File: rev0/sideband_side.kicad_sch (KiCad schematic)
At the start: 28 parts, among them IC1 ECP5-BGA256, U8 USB3343-CP

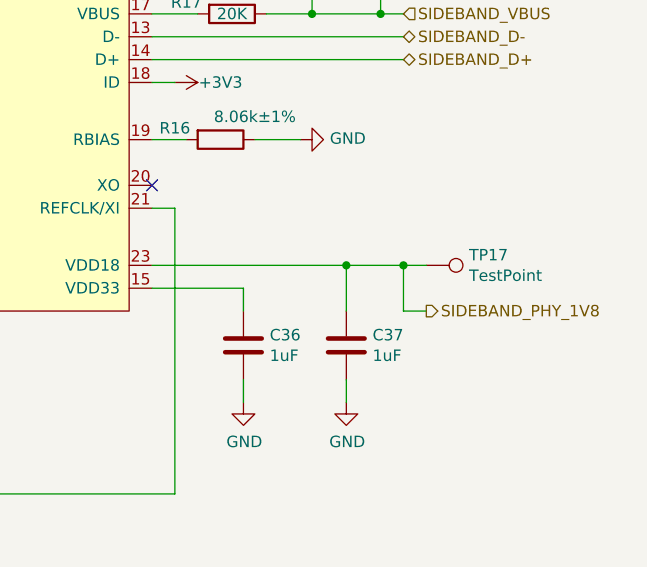
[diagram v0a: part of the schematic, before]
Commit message: hardware: remove PHY 1.8 V measurement
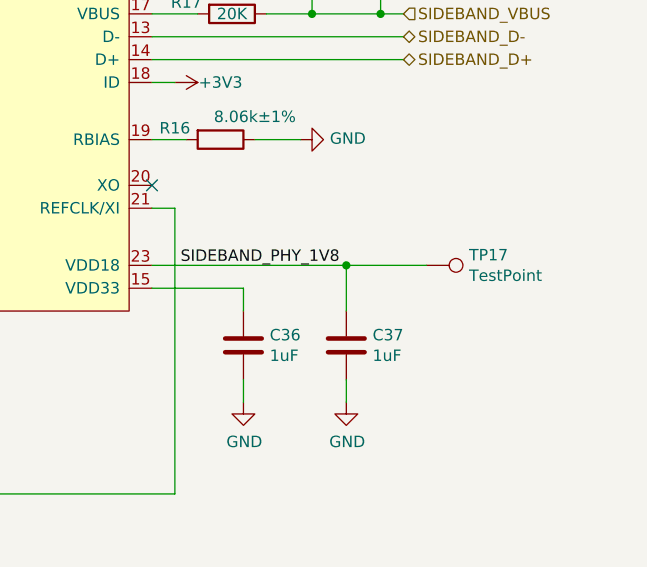
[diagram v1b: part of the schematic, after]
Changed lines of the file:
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@@
   (junction (at 33.02 64.77) (diameter 0) (color 0 0 0 0)
-  )
-  (junction (at 254 124.46) (diameter 0) (color 0 0 0 0)
   )
   (junction (at 46.99 52.07) (diameter 0) (color 0 0 0 0)
@@
     (stroke (width 0) (type default) (color 0 0 0 0))
   )
-  (wire (pts (xy 247.65 124.46) (xy 254 124.46))
+  (wire (pts (xy 247.65 124.46) (xy 256.54 124.46))
     (stroke (width 0) (type default) (color 0 0 0 0))
   )
@@
     (stroke (width 0) (type default) (color 0 0 0 0))
   )
-  (wire (pts (xy 254 124.46) (xy 256.54 124.46))
-    (stroke (width 0) (type default) (color 0 0 0 0))
-  )
   (wire (pts (xy 85.09 34.29) (xy 90.17 34.29))
     (stroke (width 0) (type default) (color 0 0 0 0))
@@
     (stroke (width 0) (type default) (color 0 0 0 0))
   )
-  (wire (pts (xy 254 129.54) (xy 254 124.46))
-    (stroke (width 0) (type default) (color 0 0 0 0))
-  )
   (wire (pts (xy 68.58 49.53) (xy 68.58 52.07))
     (stroke (width 0) (type default) (color 0 0 0 0))
@@
     (stroke (width 0) (type default) (color 0 0 0 0))
   )
-  (wire (pts (xy 256.54 129.54) (xy 254 129.54))
-    (stroke (width 0) (type default) (color 0 0 0 0))
-  )
   (wire (pts (xy 119.38 157.48) (xy 151.13 157.48))
     (stroke (width 0) (type default) (color 0 0 0 0))
@@
   )
   (label "SIDEBAND_DATA3" (at 168.91 93.98 0)
+    (effects (font (size 1.27 1.27)) (justify left bottom))
+  )
+  (label "SIDEBAND_PHY_1V8" (at 229.235 124.46 0)
     (effects (font (size 1.27 1.27)) (justify left bottom))
   )
@@
     (effects (font (size 1.27 1.27)) (justify left))
   )
-  (hierarchical_label "SIDEBAND_PHY_1V8" (shape output) (at 256.54 129.54 0)
-    (effects (font (size 1.27 1.27)) (justify left))
-  )

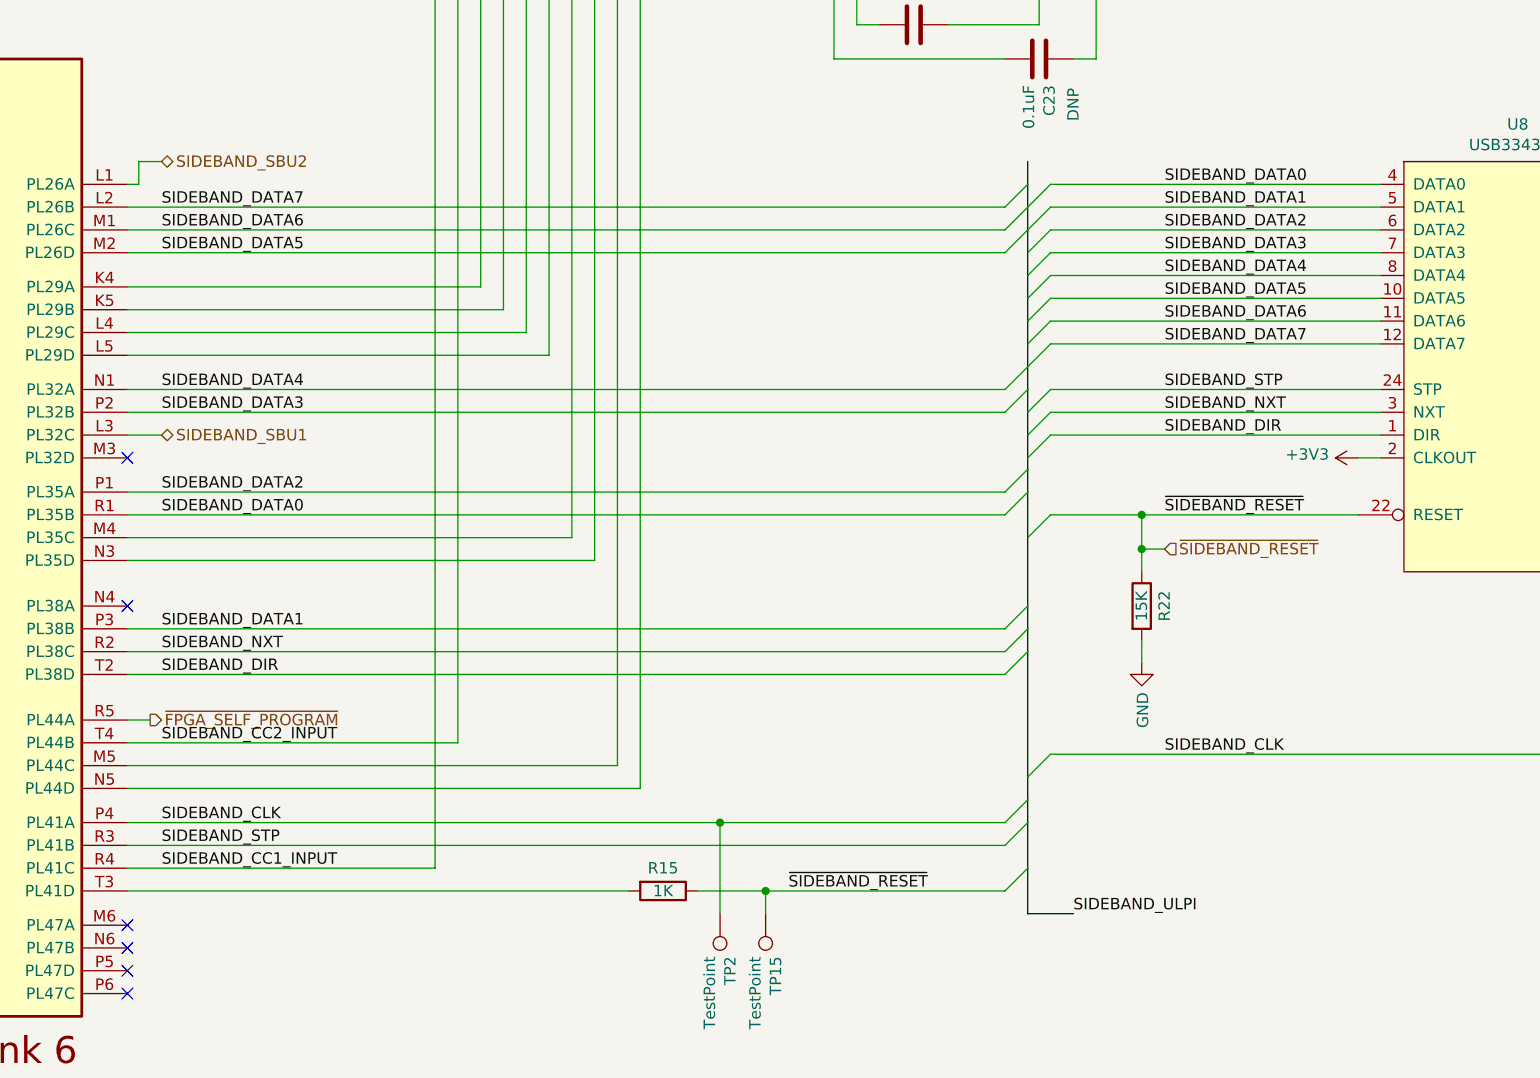
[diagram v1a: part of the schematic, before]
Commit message: hardware: rename buses for KiCad 6
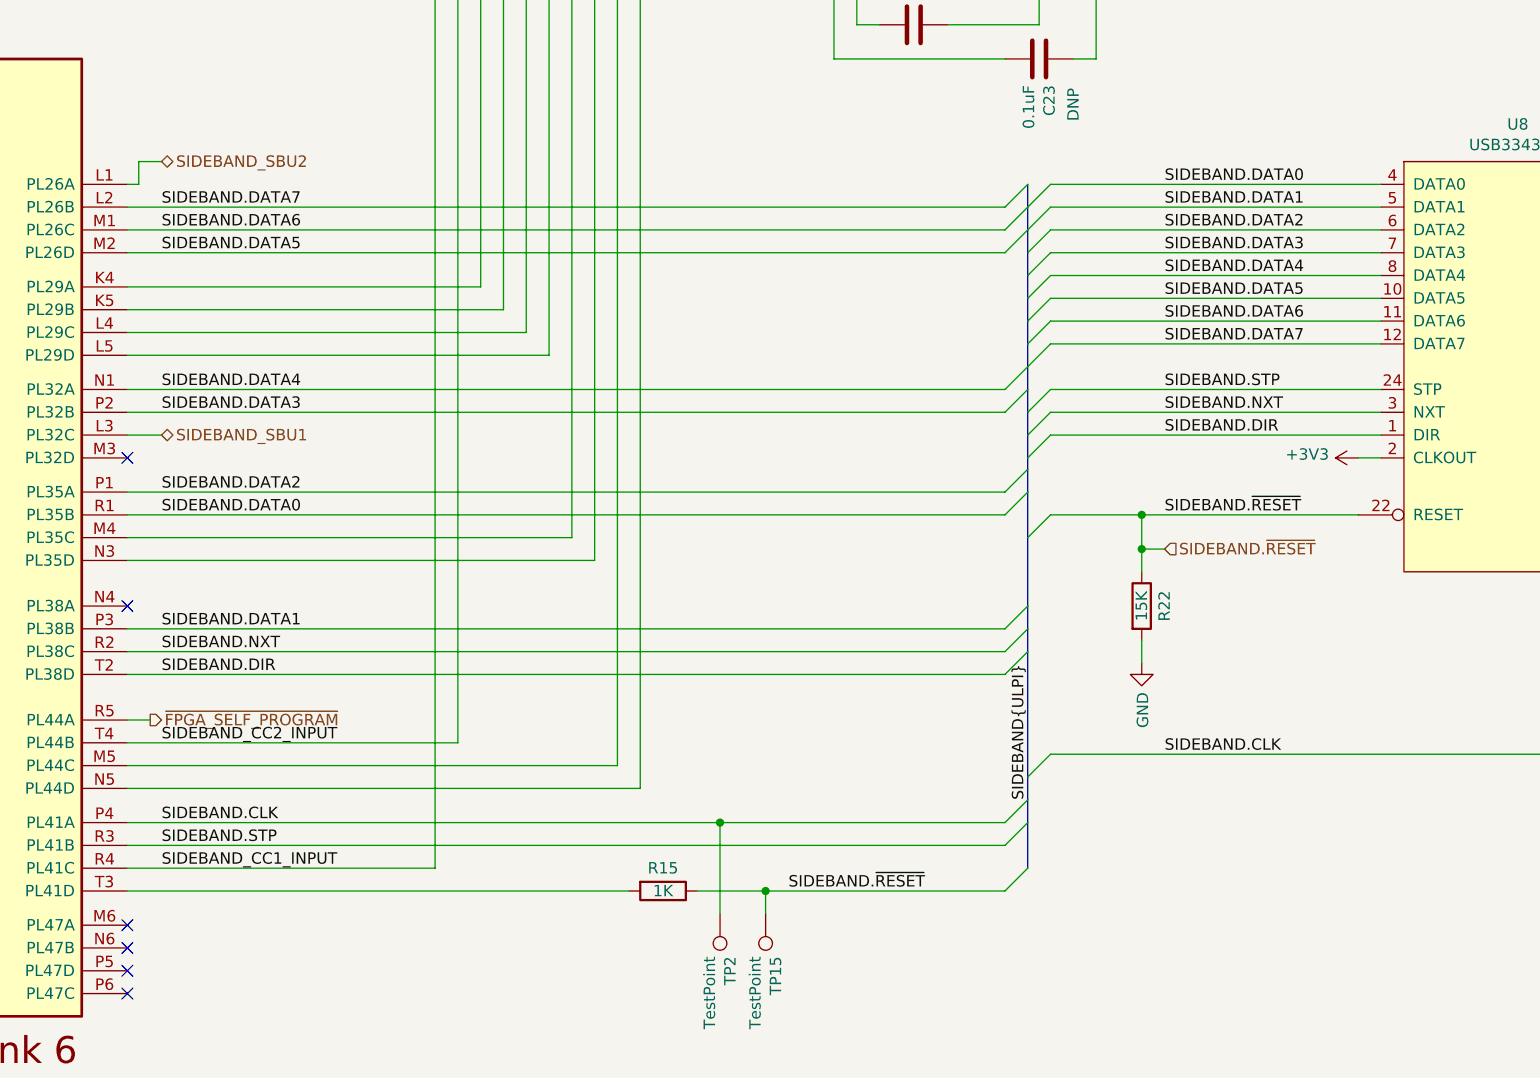
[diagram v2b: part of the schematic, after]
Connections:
- net SIDEBAND_CLK renamed SIDEBAND.CLK
- net SIDEBAND_DATA0 renamed SIDEBAND.DATA0
- net SIDEBAND_DATA1 renamed SIDEBAND.DATA1
- net SIDEBAND_DATA2 renamed SIDEBAND.DATA2
- net SIDEBAND_DATA3 renamed SIDEBAND.DATA3
- net SIDEBAND_DATA4 renamed SIDEBAND.DATA4
- net SIDEBAND_DATA5 renamed SIDEBAND.DATA5
- net SIDEBAND_DATA6 renamed SIDEBAND.DATA6
- net SIDEBAND_DATA7 renamed SIDEBAND.DATA7
- net SIDEBAND_DIR renamed SIDEBAND.DIR
- net SIDEBAND_NXT renamed SIDEBAND.NXT
- net SIDEBAND_STP renamed SIDEBAND.STP
- net ~{SIDEBAND_RESET} renamed SIDEBAND.~{RESET}
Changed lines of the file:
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@@
-    (stroke (width 0) (type default) (color 0 0 0 0))
-  )
-  (bus (pts (xy 153.67 162.56) (xy 153.67 167.64))
     (stroke (width 0) (type default) (color 0 0 0 0))
   )
@@
     (stroke (width 0) (type default) (color 0 0 0 0))
   )
-  (bus (pts (xy 153.67 83.82) (xy 153.67 86.36))
-    (stroke (width 0) (type default) (color 0 0 0 0))
-  )
   (wire (pts (xy 144.78 39.37) (xy 165.1 39.37))
     (stroke (width 0) (type default) (color 0 0 0 0))
@@
     (stroke (width 0) (type default) (color 0 0 0 0))
   )
-  (bus (pts (xy 158.75 167.64) (xy 153.67 167.64))
-    (stroke (width 0) (type default) (color 0 0 0 0))
-  )
   (bus (pts (xy 191.77 49.53) (xy 191.77 52.07))
     (stroke (width 0) (type default) (color 0 0 0 0))
@@
     (stroke (width 0) (type default) (color 0 0 0 0))
   )
-  (label "SIDEBAND_CLK" (at 57.15 157.48 0)
-    (effects (font (size 1.27 1.27)) (justify left bottom))
-  )
-  (label "SIDEBAND_DATA0" (at 57.15 123.19 0)
-    (effects (font (size 1.27 1.27)) (justify left bottom))
-  )
-  (label "SIDEBAND_ULPI" (at 158.75 167.64 0)
-    (effects (font (size 1.27 1.27)) (justify left bottom))
-  )
-  (label "SIDEBAND_DATA5" (at 168.91 99.06 0)
-    (effects (font (size 1.27 1.27)) (justify left bottom))
-  )
-  (label "SIDEBAND_STP" (at 168.91 109.22 0)
-    (effects (font (size 1.27 1.27)) (justify left bottom))
-  )
-  (label "SIDEBAND_DATA2" (at 168.91 91.44 0)
-    (effects (font (size 1.27 1.27)) (justify left bottom))
-  )
-  (label "SIDEBAND_DIR" (at 168.91 114.3 0)
-    (effects (font (size 1.27 1.27)) (justify left bottom))
-  )
-  (label "SIDEBAND_DATA4" (at 57.15 109.22 0)
+  (label "SIDEBAND.CLK" (at 57.15 157.48 0)
+    (effects (font (size 1.27 1.27)) (justify left bottom))
+  )
+  (label "SIDEBAND.DATA0" (at 57.15 123.19 0)
+    (effects (font (size 1.27 1.27)) (justify left bottom))
+  )
+  (label "SIDEBAND.DATA5" (at 168.91 99.06 0)
+    (effects (font (size 1.27 1.27)) (justify left bottom))
+  )
+  (label "SIDEBAND.STP" (at 168.91 109.22 0)
+    (effects (font (size 1.27 1.27)) (justify left bottom))
+  )
+  (label "SIDEBAND.DATA2" (at 168.91 91.44 0)
+    (effects (font (size 1.27 1.27)) (justify left bottom))
+  )
+  (label "SIDEBAND.DIR" (at 168.91 114.3 0)
+    (effects (font (size 1.27 1.27)) (justify left bottom))
+  )
+  (label "SIDEBAND.DATA4" (at 57.15 109.22 0)
     (effects (font (size 1.27 1.27)) (justify left bottom))
   )
@@
     (effects (font (size 1.27 1.27)) (justify left bottom))
   )
-  (label "SIDEBAND_DATA3" (at 168.91 93.98 0)
+  (label "SIDEBAND.DATA3" (at 168.91 93.98 0)
     (effects (font (size 1.27 1.27)) (justify left bottom))
   )
@@
     (effects (font (size 1.27 1.27)) (justify left bottom))
   )
-  (label "SIDEBAND_CLK" (at 168.91 149.86 0)
+  (label "SIDEBAND.CLK" (at 168.91 149.86 0)
     (effects (font (size 1.27 1.27)) (justify left bottom))
   )
@@
     (effects (font (size 1.27 1.27)) (justify left bottom))
   )
-  (label "SIDEBAND_DATA4" (at 168.91 96.52 0)
-    (effects (font (size 1.27 1.27)) (justify left bottom))
-  )
-  (label "SIDEBAND_DATA7" (at 57.15 88.9 0)
-    (effects (font (size 1.27 1.27)) (justify left bottom))
-  )
-  (label "SIDEBAND_DATA2" (at 57.15 120.65 0)
+  (label "SIDEBAND.DATA4" (at 168.91 96.52 0)
+    (effects (font (size 1.27 1.27)) (justify left bottom))
+  )
+  (label "SIDEBAND.DATA7" (at 57.15 88.9 0)
+    (effects (font (size 1.27 1.27)) (justify left bottom))
+  )
+  (label "SIDEBAND.DATA2" (at 57.15 120.65 0)
     (effects (font (size 1.27 1.27)) (justify left bottom))
   )
@@
     (effects (font (size 1.27 1.27)) (justify left bottom))
   )
-  (label "SIDEBAND_DIR" (at 57.15 140.97 0)
+  (label "SIDEBAND.DIR" (at 57.15 140.97 0)
     (effects (font (size 1.27 1.27)) (justify left bottom))
   )
@@
     (effects (font (size 1.27 1.27)) (justify left bottom))
   )
-  (label "SIDEBAND_DATA1" (at 57.15 135.89 0)
+  (label "SIDEBAND.DATA1" (at 57.15 135.89 0)
     (effects (font (size 1.27 1.27)) (justify left bottom))
   )
@@
     (effects (font (size 1.27 1.27)) (justify left bottom))
   )
-  (label "SIDEBAND_DATA1" (at 168.91 88.9 0)
-    (effects (font (size 1.27 1.27)) (justify left bottom))
-  )
-  (label "SIDEBAND_STP" (at 57.15 160.02 0)
-    (effects (font (size 1.27 1.27)) (justify left bottom))
-  )
-  (label "SIDEBAND_DATA6" (at 57.15 91.44 0)
-    (effects (font (size 1.27 1.27)) (justify left bottom))
-  )
-  (label "SIDEBAND_DATA0" (at 168.91 86.36 0)
-    (effects (font (size 1.27 1.27)) (justify left bottom))
-  )
-  (label "SIDEBAND_DATA5" (at 57.15 93.98 0)
-    (effects (font (size 1.27 1.27)) (justify left bottom))
-  )
-  (label "SIDEBAND_NXT" (at 168.91 111.76 0)
-    (effects (font (size 1.27 1.27)) (justify left bottom))
-  )
-  (label "SIDEBAND_DATA6" (at 168.91 101.6 0)
-    (effects (font (size 1.27 1.27)) (justify left bottom))
-  )
-  (label "~{SIDEBAND_RESET}" (at 168.91 123.19 0)
+  (label "SIDEBAND.DATA1" (at 168.91 88.9 0)
+    (effects (font (size 1.27 1.27)) (justify left bottom))
+  )
+  (label "SIDEBAND.STP" (at 57.15 160.02 0)
+    (effects (font (size 1.27 1.27)) (justify left bottom))
+  )
+  (label "SIDEBAND.DATA6" (at 57.15 91.44 0)
+    (effects (font (size 1.27 1.27)) (justify left bottom))
+  )
+  (label "SIDEBAND{ULPI}" (at 153.67 154.94 90)
+    (effects (font (size 1.27 1.27)) (justify left bottom))
+  )
+  (label "SIDEBAND.DATA0" (at 168.91 86.36 0)
+    (effects (font (size 1.27 1.27)) (justify left bottom))
+  )
+  (label "SIDEBAND.DATA5" (at 57.15 93.98 0)
+    (effects (font (size 1.27 1.27)) (justify left bottom))
+  )
+  (label "SIDEBAND.NXT" (at 168.91 111.76 0)
+    (effects (font (size 1.27 1.27)) (justify left bottom))
+  )
+  (label "SIDEBAND.DATA6" (at 168.91 101.6 0)
+    (effects (font (size 1.27 1.27)) (justify left bottom))
+  )
+  (label "SIDEBAND.~{RESET}" (at 168.91 123.19 0)
     (effects (font (size 1.27 1.27)) (justify left bottom))
   )
@@
     (effects (font (size 1.27 1.27)) (justify left bottom))
   )
-  (label "SIDEBAND_NXT" (at 57.15 138.43 0)
+  (label "SIDEBAND.NXT" (at 57.15 138.43 0)
     (effects (font (size 1.27 1.27)) (justify left bottom))
   )
@@
     (effects (font (size 1.27 1.27)) (justify left bottom))
   )
-  (label "~{SIDEBAND_RESET}" (at 127 165.1 0)
-    (effects (font (size 1.27 1.27)) (justify left bottom))
-  )
-  (label "SIDEBAND_DATA7" (at 168.91 104.14 0)
-    (effects (font (size 1.27 1.27)) (justify left bottom))
-  )
-  (label "SIDEBAND_DATA3" (at 57.15 111.76 0)
+  (label "SIDEBAND.~{RESET}" (at 127 165.1 0)
+    (effects (font (size 1.27 1.27)) (justify left bottom))
+  )
+  (label "SIDEBAND.DATA7" (at 168.91 104.14 0)
+    (effects (font (size 1.27 1.27)) (justify left bottom))
+  )
+  (label "SIDEBAND.DATA3" (at 57.15 111.76 0)
     (effects (font (size 1.27 1.27)) (justify left bottom))
   )
@@
     (effects (font (size 1.27 1.27)) (justify right))
   )
-  (hierarchical_label "~{SIDEBAND_RESET}" (shape input) (at 168.91 127 0)
+  (hierarchical_label "SIDEBAND.~{RESET}" (shape input) (at 168.91 127 0)
     (effects (font (size 1.27 1.27)) (justify left))
   )

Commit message: hardware: use DNP field for DNP notation
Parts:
- C19, C21, C23, C5, TP15, TP16, TP17, TP2, TP38, TP39: DNP (none) -> DNP; Note DNP -> (none)
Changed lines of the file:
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@@
       (effects (font (size 1.27 1.27)) hide)
     )
-    (property "Note" "DNP" (id 6) (at 158.75 48.26 0))
+    (property "DNP" "DNP" (id 6) (at 158.75 48.26 0))
     (pin "1")
     (pin "2")
@@
       (effects (font (size 1.27 1.27)) hide)
     )
-    (property "Note" "DNP" (id 6) (at 144.78 34.29 0))
+    (property "DNP" "DNP" (id 6) (at 144.78 34.29 0))
     (pin "1")
     (pin "2")
@@
       (effects (font (size 1.27 1.27)) hide)
     )
-    (property "Note" "DNP" (id 6) (at 144.78 63.5 0))
+    (property "DNP" "DNP" (id 6) (at 144.78 63.5 0))
     (pin "1")
     (pin "2")
@@
       (effects (font (size 1.27 1.27)) hide)
     )
-    (property "Note" "DNP" (id 6) (at 158.75 77.47 0))
+    (property "DNP" "DNP" (id 6) (at 158.75 77.47 0))
     (pin "1")
     (pin "2")
@@
       (effects (font (size 1.27 1.27)) hide)
     )
-    (property "Note" "DNP" (id 4) (at 52.07 31.75 0)
+    (property "DNP" "DNP" (id 4) (at 52.07 31.75 0)
       (effects (font (size 1.27 1.27)) hide)
     )
@@
       (effects (font (size 1.27 1.27)) hide)
     )
-    (property "Note" "DNP" (id 4) (at 57.15 31.75 0)
+    (property "DNP" "DNP" (id 4) (at 57.15 31.75 0)
       (effects (font (size 1.27 1.27)) hide)
     )
@@
       (effects (font (size 1.27 1.27)) hide)
     )
-    (property "Note" "DNP" (id 4) (at 256.54 124.46 0)
+    (property "DNP" "DNP" (id 4) (at 256.54 124.46 0)
       (effects (font (size 1.27 1.27)) hide)
     )
@@
       (effects (font (size 1.27 1.27)) hide)
     )
-    (property "Note" "DNP" (id 4) (at 251.46 93.98 0)
+    (property "DNP" "DNP" (id 4) (at 251.46 93.98 0)
       (effects (font (size 1.27 1.27)) hide)
     )
@@
       (effects (font (size 1.27 1.27)) hide)
     )
-    (property "Note" "DNP" (id 4) (at 124.46 167.64 0)
+    (property "DNP" "DNP" (id 4) (at 124.46 167.64 0)
       (effects (font (size 1.27 1.27)) hide)
     )
@@
       (effects (font (size 1.27 1.27)) hide)
     )
-    (property "Note" "DNP" (id 4) (at 119.38 167.64 0)
-      (effects (font (size 1.27 1.27)) hide)
-    )
+    (property "DNP" "DNP" (id 4) (at 119.38 167.64 0)
+      (effects (font (size 1.27 1.27)) hide)
+    )
